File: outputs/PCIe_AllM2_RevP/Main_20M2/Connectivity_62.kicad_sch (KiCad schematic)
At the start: 2 parts, among them Y701 38.4MHz crystal / load and ES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, Y702 32.768kHz crystal / load and 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

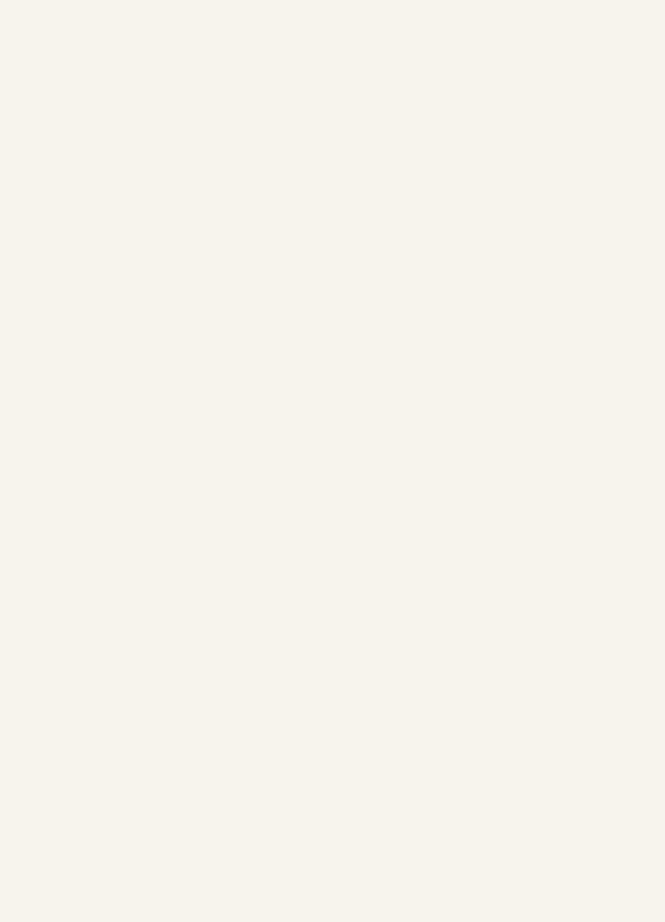
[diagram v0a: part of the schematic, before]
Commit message: Repair Rev P reset bias, native parity and netclass validation
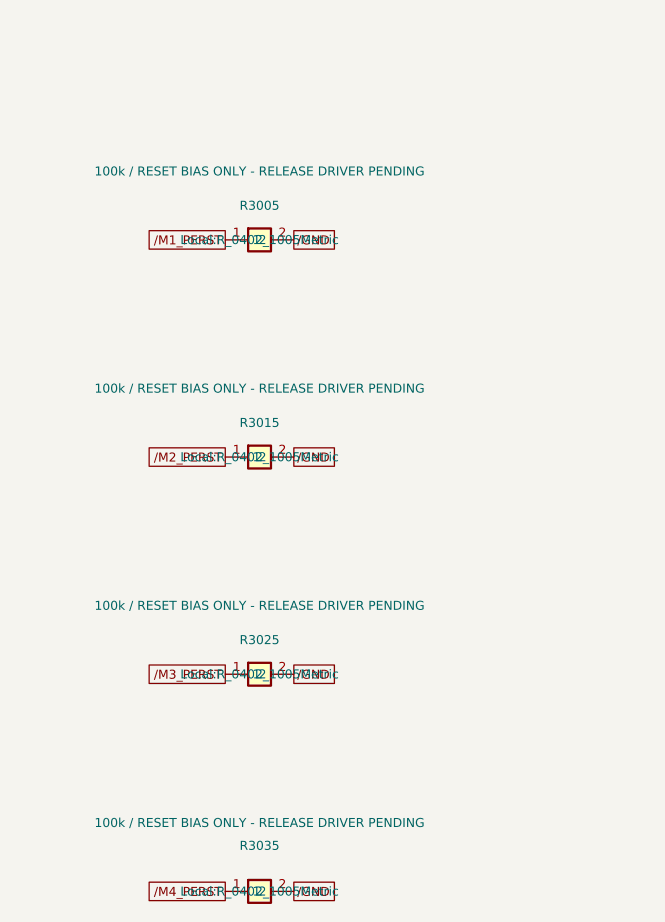
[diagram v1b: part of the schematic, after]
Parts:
- added R3005: 100k / RESET BIAS ONLY - RELEASE DRIVER PENDING, Local:R_0402_1005Metric, symbol Local:PART_R3005
- added R3015: 100k / RESET BIAS ONLY - RELEASE DRIVER PENDING, Local:R_0402_1005Metric, symbol Local:PART_R3015
- added R3025: 100k / RESET BIAS ONLY - RELEASE DRIVER PENDING, Local:R_0402_1005Metric, symbol Local:PART_R3025
- added R3035: 100k / RESET BIAS ONLY - RELEASE DRIVER PENDING, Local:R_0402_1005Metric, symbol Local:PART_R3035
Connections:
- net /GND: now also R3005.2, R3015.2, R3025.2, R3035.2
- new net /M1_PERST: R3005.1
- new net /M2_PERST: R3015.1
- new net /M3_PERST: R3025.1
- new net /M4_PERST: R3035.1
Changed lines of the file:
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@@
 (global_label "/CPU_RTCX1" (shape passive) (at 203.2 73.66 180) (effects (font (size 0.8 0.8)) (justify right)))
 (global_label "/CPU_RTCX2" (shape passive) (at 233.68 73.66 0) (effects (font (size 0.8 0.8)) (justify left)))
+(symbol (lib_id "Local:PART_R3005") (at 74.93 170.18 0) (unit 1) (in_bom yes) (on_board yes) (dnp no)
+(property "Reference" "R3005" (at 74.93 166.37 0) (effects (font (size 1 1))))(property "Value" "100k / RESET BIAS ONLY - RELEASE DRIVER PENDING" (at 74.93 162.56 0) (effects (font (size 1 1))))(property "Footprint" "Local:R_0402_1005Metric" (at 74.93 170.18 0) (effects (font (size 1 1))))
+(pin "1")(pin "2")
+(instances (project "Main_20M2" (path "/5ced22a3-fbbf-4a15-9c67-0373c30eb779/143d1ce0-4ca8-45ee-8c53-bfa17bf3b25d" (reference "R3005") (unit 1)))))
+(global_label "/M1_PERST" (shape passive) (at 71.12 170.18 180) (effects (font (size 1 1))))
+(global_label "/GND" (shape passive) (at 78.74 170.18 0) (effects (font (size 1 1))))
+(symbol (lib_id "Local:PART_R3015") (at 74.93 194.31 0) (unit 1) (in_bom yes) (on_board yes) (dnp no)
+(property "Reference" "R3015" (at 74.93 190.5 0) (effects (font (size 1 1))))(property "Value" "100k / RESET BIAS ONLY - RELEASE DRIVER PENDING" (at 74.93 186.69 0) (effects (font (size 1 1))))(property "Footprint" "Local:R_0402_1005Metric" (at 74.93 194.31 0) (effects (font (size 1 1))))
+(pin "1")(pin "2")
+(instances (project "Main_20M2" (path "/5ced22a3-fbbf-4a15-9c67-0373c30eb779/143d1ce0-4ca8-45ee-8c53-bfa17bf3b25d" (reference "R3015") (unit 1)))))
+(global_label "/M2_PERST" (shape passive) (at 71.12 194.31 180) (effects (font (size 1 1))))
+(global_label "/GND" (shape passive) (at 78.74 194.31 0) (effects (font (size 1 1))))
+(symbol (lib_id "Local:PART_R3025") (at 74.93 218.44 0) (unit 1) (in_bom yes) (on_board yes) (dnp no)
+(property "Reference" "R3025" (at 74.93 214.63 0) (effects (font (size 1 1))))(property "Value" "100k / RESET BIAS ONLY - RELEASE DRIVER PENDING" (at 74.93 210.82 0) (effects (font (size 1 1))))(property "Footprint" "Local:R_0402_1005Metric" (at 74.93 218.44 0) (effects (font (size 1 1))))
+(pin "1")(pin "2")
+(instances (project "Main_20M2" (path "/5ced22a3-fbbf-4a15-9c67-0373c30eb779/143d1ce0-4ca8-45ee-8c53-bfa17bf3b25d" (reference "R3025") (unit 1)))))
+(global_label "/M3_PERST" (shape passive) (at 71.12 218.44 180) (effects (font (size 1 1))))
+(global_label "/GND" (shape passive) (at 78.74 218.44 0) (effects (font (size 1 1))))
+(symbol (lib_id "Local:PART_R3035") (at 74.93 242.57 0) (unit 1) (in_bom yes) (on_board yes) (dnp no)
+(property "Reference" "R3035" (at 74.93 237.49 0) (effects (font (size 1 1))))(property "Value" "100k / RESET BIAS ONLY - RELEASE DRIVER PENDING" (at 74.93 234.95000000000002 0) (effects (font (size 1 1))))(property "Footprint" "Local:R_0402_1005Metric" (at 74.93 242.57 0) (effects (font (size 1 1))))
+(pin "1")(pin "2")
+(instances (project "Main_20M2" (path "/5ced22a3-fbbf-4a15-9c67-0373c30eb779/143d1ce0-4ca8-45ee-8c53-bfa17bf3b25d" (reference "R3035") (unit 1)))))
+(global_label "/M4_PERST" (shape passive) (at 71.12 242.57 180) (effects (font (size 1 1))))
+(global_label "/GND" (shape passive) (at 78.74 242.57 0) (effects (font (size 1 1))))
 )
